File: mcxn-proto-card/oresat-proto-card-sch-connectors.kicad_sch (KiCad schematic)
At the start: 11 parts, among them J1 J-SAMTEC-TFM-110-01-L-D-RA, J2 U.FL, J3 U.FL, J4 U.FL, J6 J-SAMTEC-TFM-120-X1-XXX-D-RA

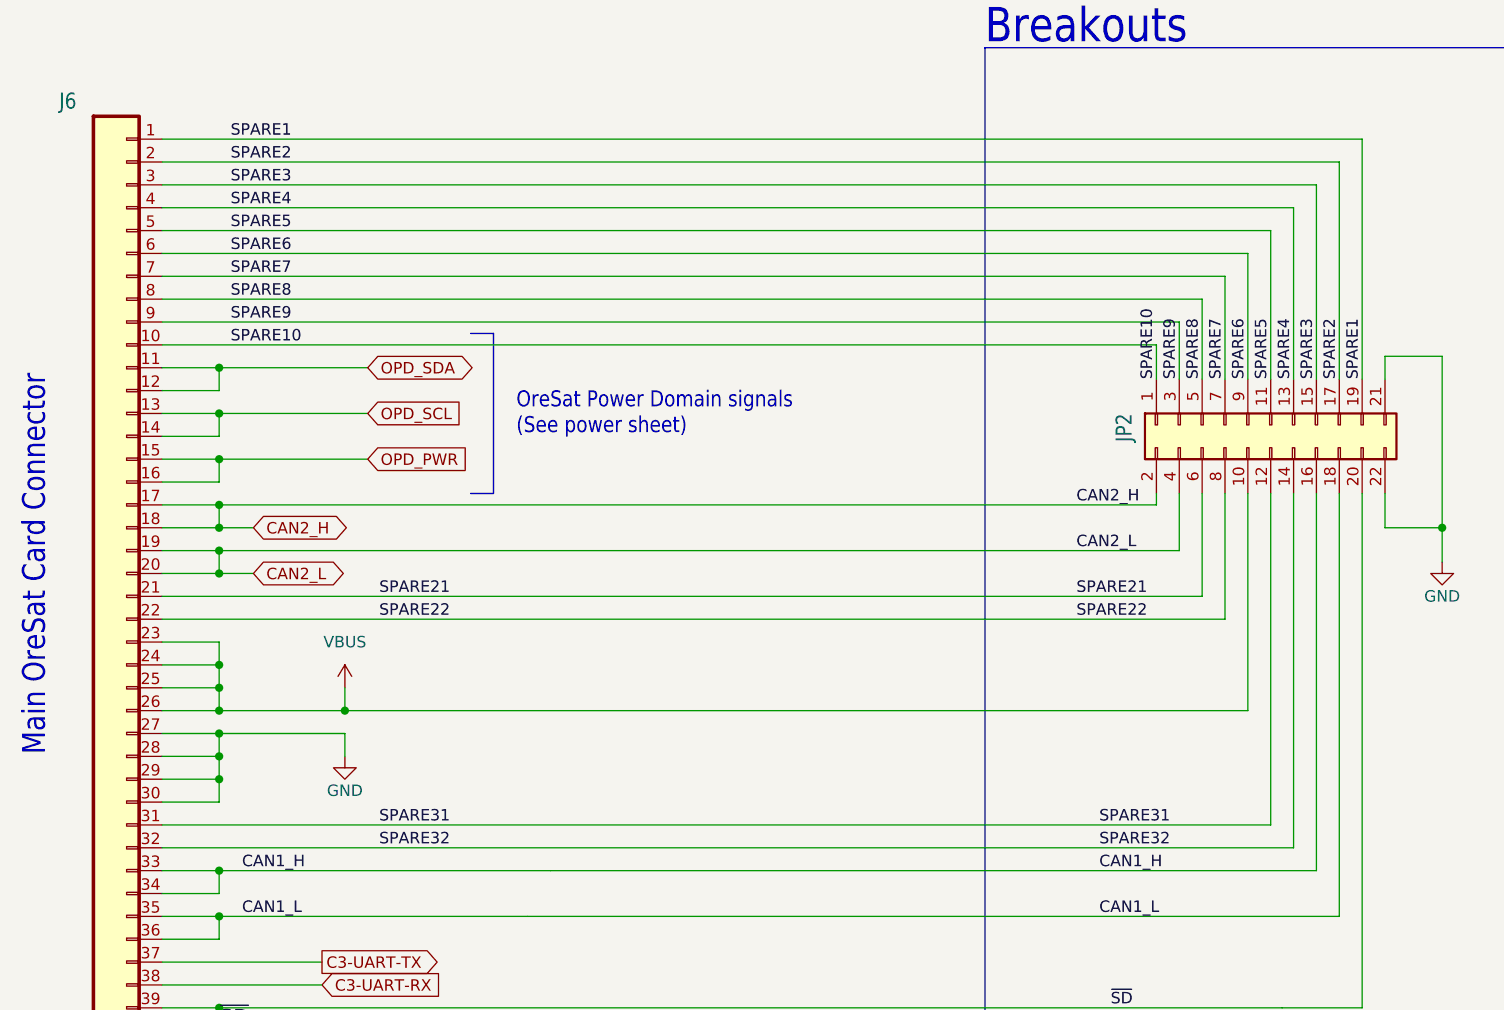
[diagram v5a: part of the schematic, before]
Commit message: changed layout
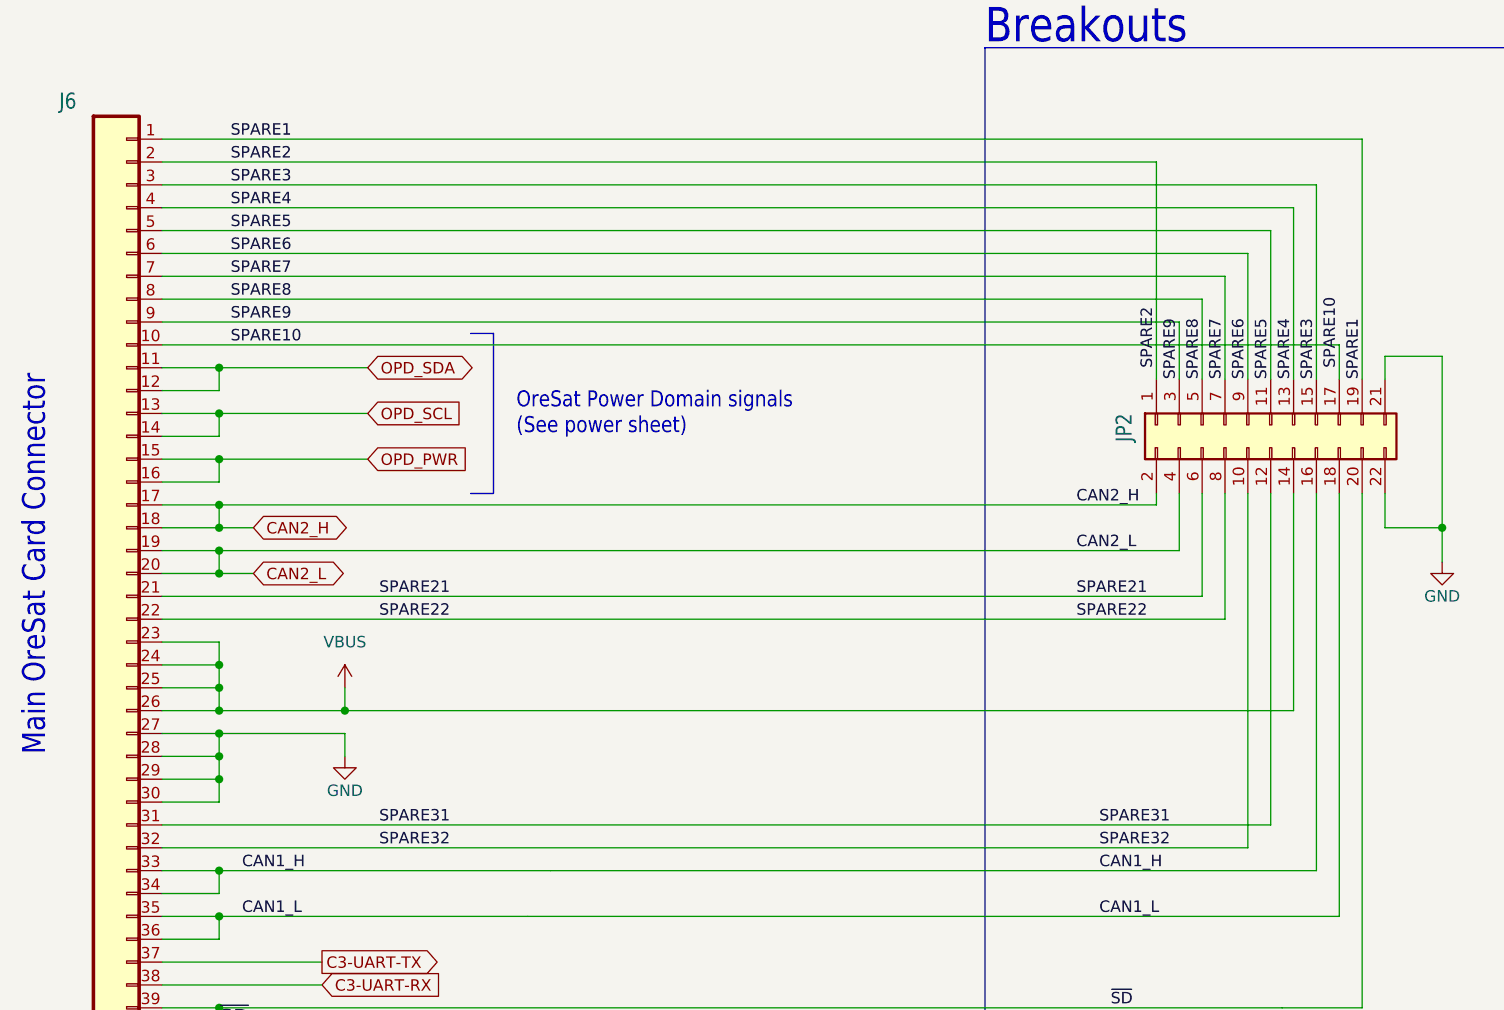
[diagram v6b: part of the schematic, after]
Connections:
- net SPARE10: now also JP2.17 (Pin_17); no longer JP2.1 (Pin_1)
- net SPARE2: now also JP2.1 (Pin_1); no longer JP2.17 (Pin_17)
- net SPARE32: now also JP2.10 (Pin_10); no longer JP2.14 (Pin_14)
- net VBUS: now also JP2.14 (Pin_14); no longer JP2.10 (Pin_10)
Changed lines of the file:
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@@
 	(wire
 		(pts
-			(xy 78.74 71.12) (xy 189.23 71.12)
+			(xy 78.74 71.12) (xy 209.55 71.12)
 		)
 		(stroke
@@
 	(wire
 		(pts
+			(xy 199.39 87.63) (xy 199.39 127)
+		)
+		(stroke
+			(width 0)
+			(type default)
+		)
+	)
+	(wire
+		(pts
 			(xy 196.85 101.6) (xy 196.85 87.63)
 		)
@@
 	(wire
 		(pts
-			(xy 199.39 87.63) (xy 199.39 111.76)
-		)
-		(stroke
-			(width 0.1524)
-			(type solid)
-		)
-	)
-	(wire
-		(pts
 			(xy 99.06 114.3) (xy 99.06 116.84)
 		)
@@
 	(wire
 		(pts
-			(xy 209.55 74.93) (xy 209.55 50.8)
-		)
-		(stroke
-			(width 0)
-			(type default)
-		)
-	)
-	(wire
-		(pts
 			(xy 194.31 74.93) (xy 194.31 66.04)
 		)
@@
 	(wire
 		(pts
+			(xy 189.23 50.8) (xy 189.23 74.93)
+		)
+		(stroke
+			(width 0.1524)
+			(type solid)
+		)
+	)
+	(wire
+		(pts
 			(xy 86.36 180.34) (xy 114.3 180.34)
 		)
@@
 	(wire
 		(pts
+			(xy 204.47 87.63) (xy 204.47 111.76)
+		)
+		(stroke
+			(width 0.1524)
+			(type solid)
+		)
+	)
+	(wire
+		(pts
 			(xy 297.18 152.4) (xy 297.18 154.94)
 		)
@@
 	(wire
 		(pts
-			(xy 99.06 111.76) (xy 199.39 111.76)
+			(xy 99.06 111.76) (xy 204.47 111.76)
 		)
 		(stroke
@@
 	(wire
 		(pts
+			(xy 209.55 71.12) (xy 209.55 74.93)
+		)
+		(stroke
+			(width 0)
+			(type default)
+		)
+	)
+	(wire
+		(pts
 			(xy 78.74 139.7) (xy 96.52 139.7)
 		)
@@
 	(wire
 		(pts
-			(xy 204.47 87.63) (xy 204.47 127)
-		)
-		(stroke
-			(width 0)
-			(type default)
-		)
-	)
-	(wire
-		(pts
 			(xy 78.74 165.1) (xy 86.36 165.1)
 		)
@@
 	(wire
 		(pts
-			(xy 78.74 127) (xy 204.47 127)
+			(xy 78.74 127) (xy 199.39 127)
 		)
 		(stroke
@@
 	(wire
 		(pts
-			(xy 78.74 50.8) (xy 209.55 50.8)
-		)
-		(stroke
-			(width 0.1524)
-			(type solid)
-		)
-	)
-	(wire
-		(pts
-			(xy 189.23 74.93) (xy 189.23 71.12)
-		)
-		(stroke
-			(width 0)
-			(type default)
+			(xy 78.74 50.8) (xy 189.23 50.8)
+		)
+		(stroke
+			(width 0.1524)
+			(type solid)
 		)
 	)
@@
 		)
 	)
+	(label "SPARE2"
+		(at 189.23 73.66 90)
+		(effects
+			(font
+				(size 1.27 1.27)
+			)
+			(justify left bottom)
+		)
+	)
 	(label "AUX-3"
 		(at 88.9 175.26 0)
@@
 		)
 	)
+	(label "SPARE10"
+		(at 209.55 73.66 90)
+		(effects
+			(font
+				(size 1.27 1.27)
+			)
+			(justify left bottom)
+		)
+	)
 	(label "SPARE4"
 		(at 204.47 74.93 90)
@@
 			)
 			(justify left bottom)
-		)
-	)
-	(label "SPARE10"
-		(at 189.23 74.93 90)
-		(effects
-			(font
-				(size 1.27 1.27)
-			)
-			(justify left bottom)
-		)
-	)
-	(label "SPARE2"
-		(at 209.55 74.93 90)
-		(effects
-			(font
-				(size 1.27 1.27)
-			)
-			(justify left bottom)

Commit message: Fixed linked library footprints and routing
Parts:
- JP2: footprint Connector_PinHeader_2.54mm:PinHeader_2x12_P2.54mm_Vertical -> Connector_PinHeader_2.54mm:PinHeader_2x11_P2.54mm_Vertical; DIS Digi-Key -> (none); DPN 609-3243-ND -> (none); MFR Amphenol -> (none); MPN 67997-410HLF -> (none)
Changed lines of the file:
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@@
 			)
 		)
-		(property "Footprint" "Connector_PinHeader_2.54mm:PinHeader_2x12_P2.54mm_Vertical"
+		(property "Footprint" "Connector_PinHeader_2.54mm:PinHeader_2x11_P2.54mm_Vertical"
 			(at 201.93 80.01 0)
 			(effects
@@
 			)
 		)
-		(property "DIS" "Digi-Key"
+		(property "DIS" ""
 			(at 201.93 80.01 0)
 			(effects
@@
 			)
 		)
-		(property "DPN" "609-3243-ND"
+		(property "DPN" ""
 			(at 201.93 80.01 0)
 			(effects
@@
 			)
 		)
-		(property "MFR" "Amphenol "
+		(property "MFR" ""
 			(at 201.93 80.01 0)
 			(effects
@@
 			)
 		)
-		(property "MPN" "67997-410HLF"
+		(property "MPN" ""
 			(at 201.93 80.01 0)
 			(effects

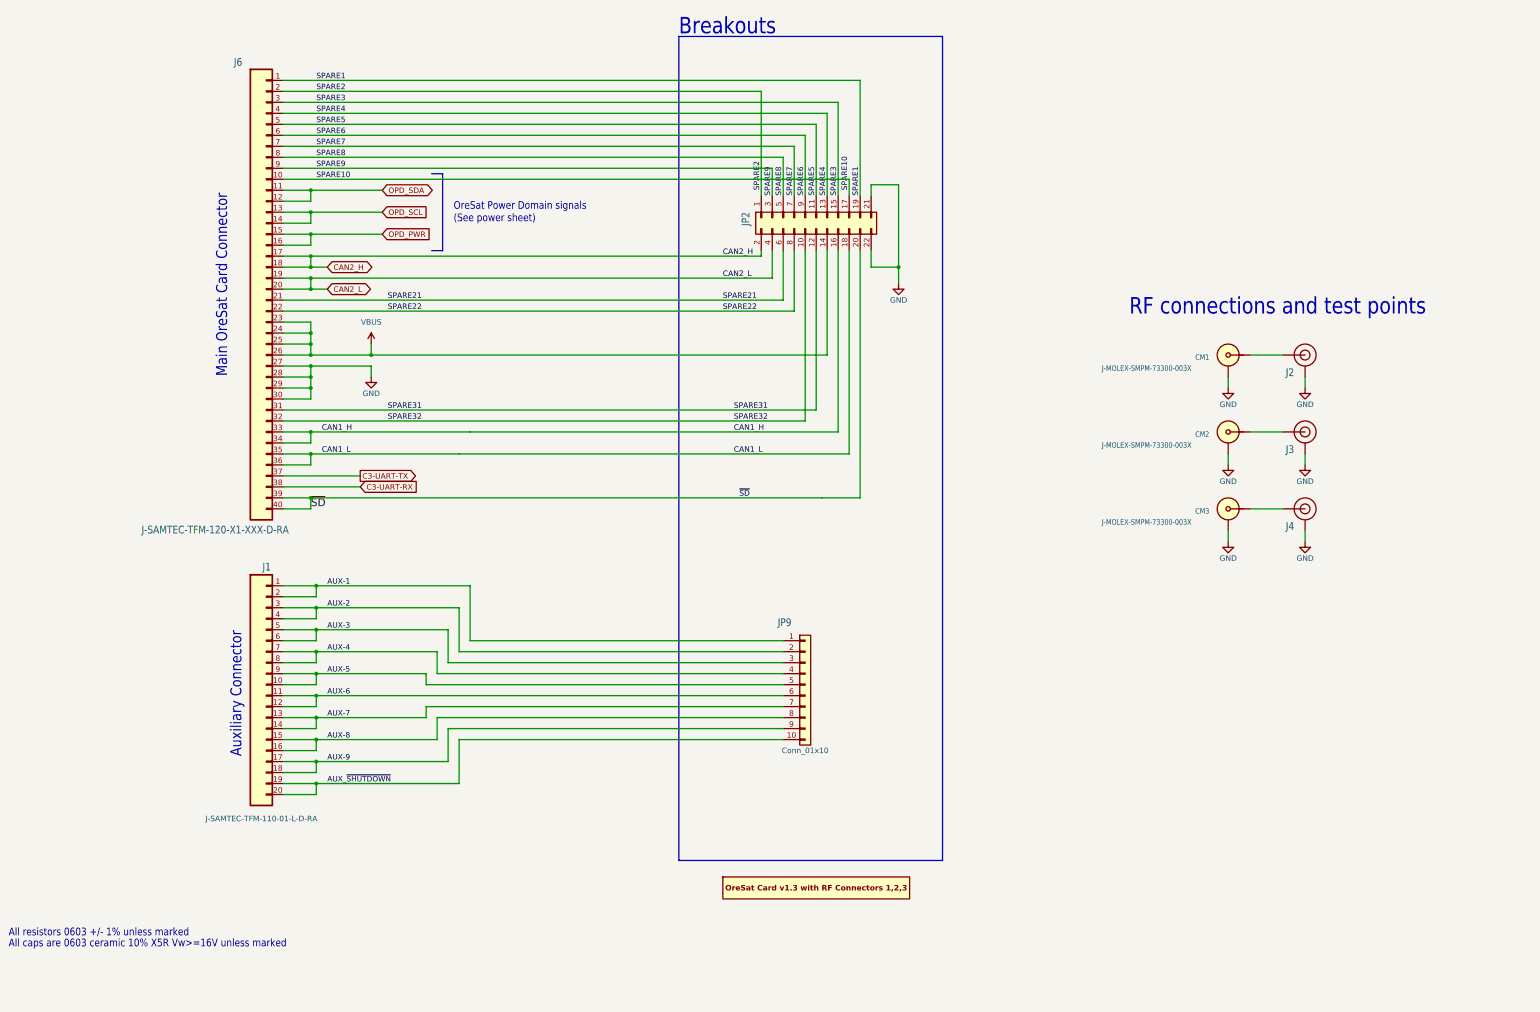
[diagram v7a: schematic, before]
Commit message: Fixed schematic and routing for 2x11 connector
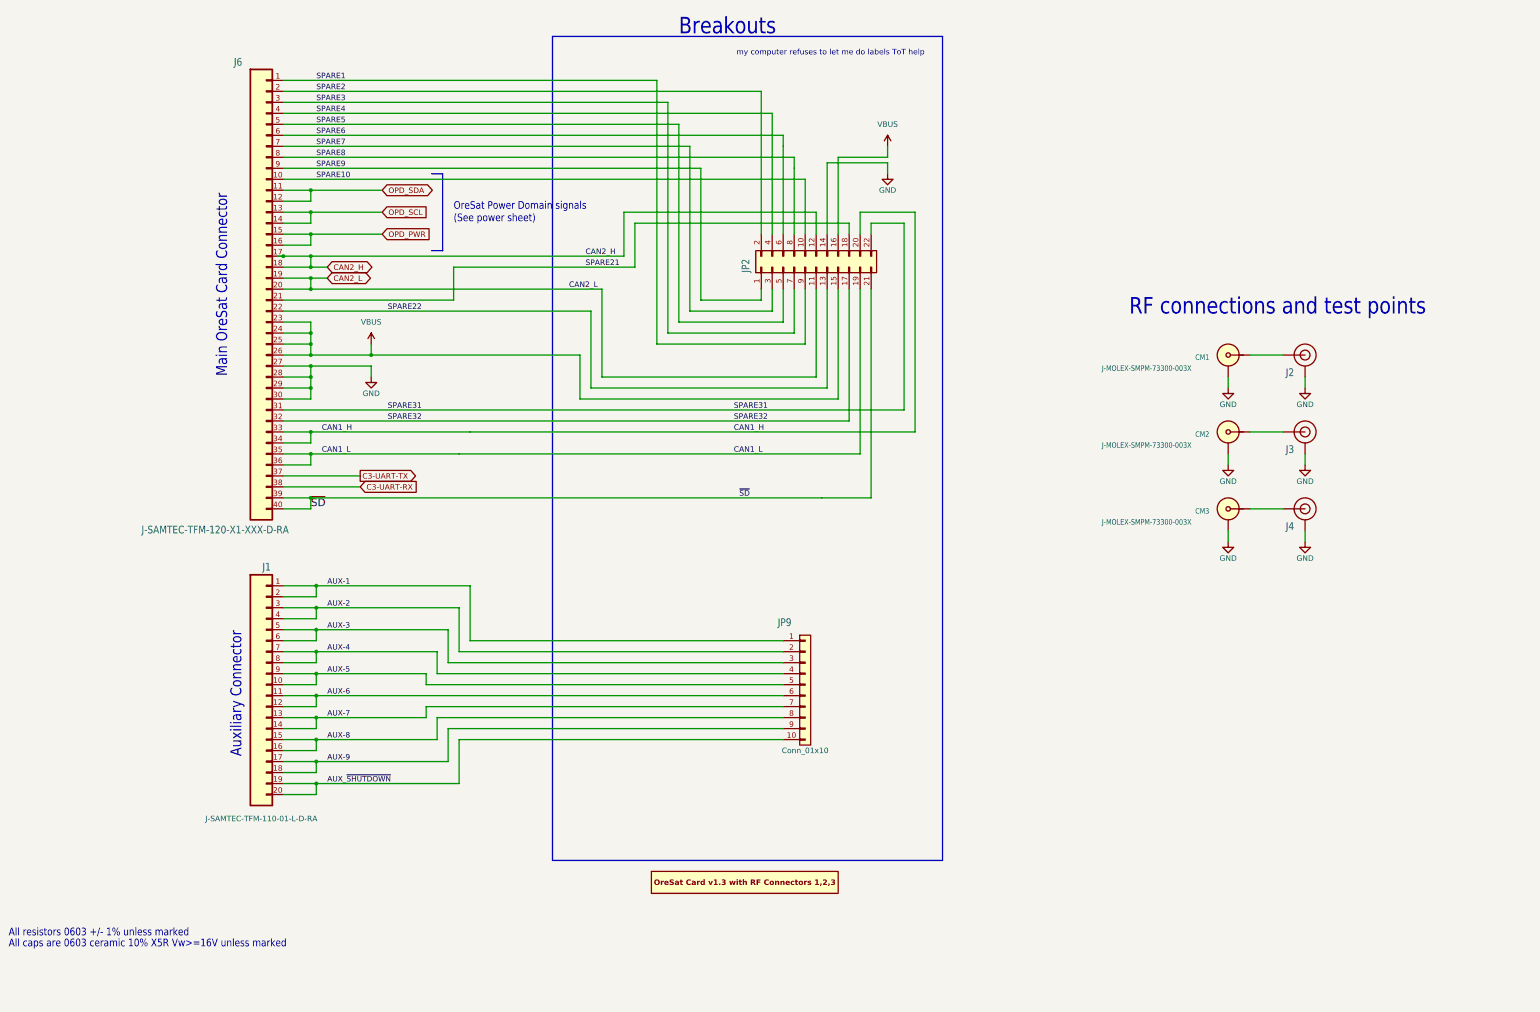
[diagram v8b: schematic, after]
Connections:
- net CAN1_H: now also JP2.20 (Pin_20); no longer JP2.16 (Pin_16)
- net CAN1_L: now also JP2.19 (Pin_19); no longer JP2.18 (Pin_18)
- net CAN2_H: now also JP2.12 (Pin_12); no longer JP2.2 (Pin_2)
- net CAN2_L: now also JP2.11 (Pin_11); no longer JP2.4 (Pin_4)
- net GND: now also JP2.14 (Pin_14); no longer JP2.21 (Pin_21), JP2.22 (Pin_22)
- net SPARE1: now also JP2.9 (Pin_9); no longer JP2.19 (Pin_19)
- net SPARE10: now also JP2.10 (Pin_10); no longer JP2.17 (Pin_17)
- net SPARE2: now also JP2.2 (Pin_2); no longer JP2.1 (Pin_1)
- net SPARE21: now also JP2.18 (Pin_18); no longer JP2.6 (Pin_6)
- net SPARE22: now also JP2.13 (Pin_13); no longer JP2.8 (Pin_8)
- net SPARE3: now also JP2.7 (Pin_7); no longer JP2.15 (Pin_15)
- net SPARE31: now also JP2.22 (Pin_22); no longer JP2.12 (Pin_12)
- net SPARE32: now also JP2.17 (Pin_17); no longer JP2.10 (Pin_10)
- net SPARE4: now also JP2.4 (Pin_4); no longer JP2.13 (Pin_13)
- net SPARE5: now also JP2.5 (Pin_5); no longer JP2.11 (Pin_11)
- net SPARE6: now also JP2.6 (Pin_6); no longer JP2.9 (Pin_9)
- net SPARE7: now also JP2.3 (Pin_3); no longer JP2.7 (Pin_7)
- net SPARE8: now also JP2.8 (Pin_8); no longer JP2.5 (Pin_5)
- net SPARE9: now also JP2.1 (Pin_1); no longer JP2.3 (Pin_3)
- net VBUS: now also JP2.15 (Pin_15), JP2.16 (Pin_16); no longer JP2.14 (Pin_14)
- net ~{SD}: now also JP2.21 (Pin_21); no longer JP2.20 (Pin_20)
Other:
- note added: "my computer refuses to let me do labels ToT help"
- moved on the sheet: JP2
